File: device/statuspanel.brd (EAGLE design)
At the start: 57.1 x 66 mm, 8 parts

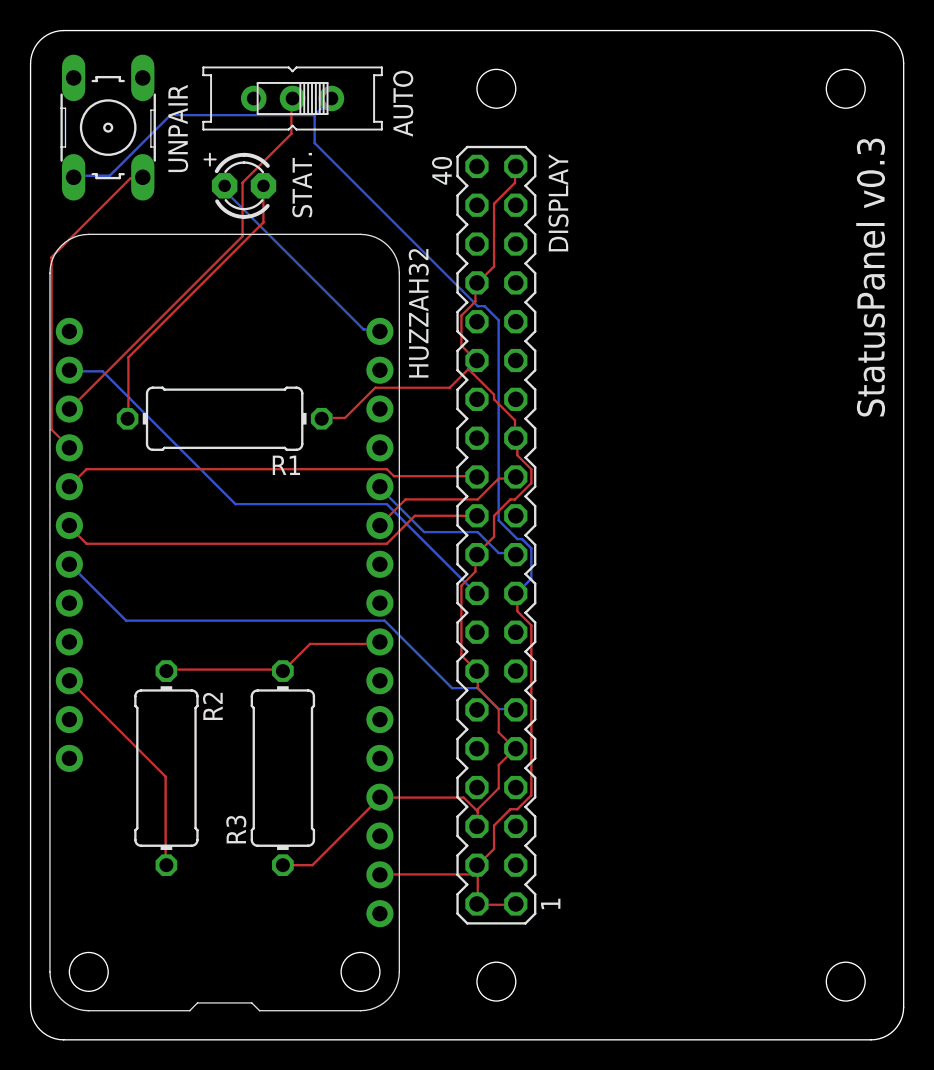
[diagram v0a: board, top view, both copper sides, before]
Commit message: Switching the resistors over to SMD components.
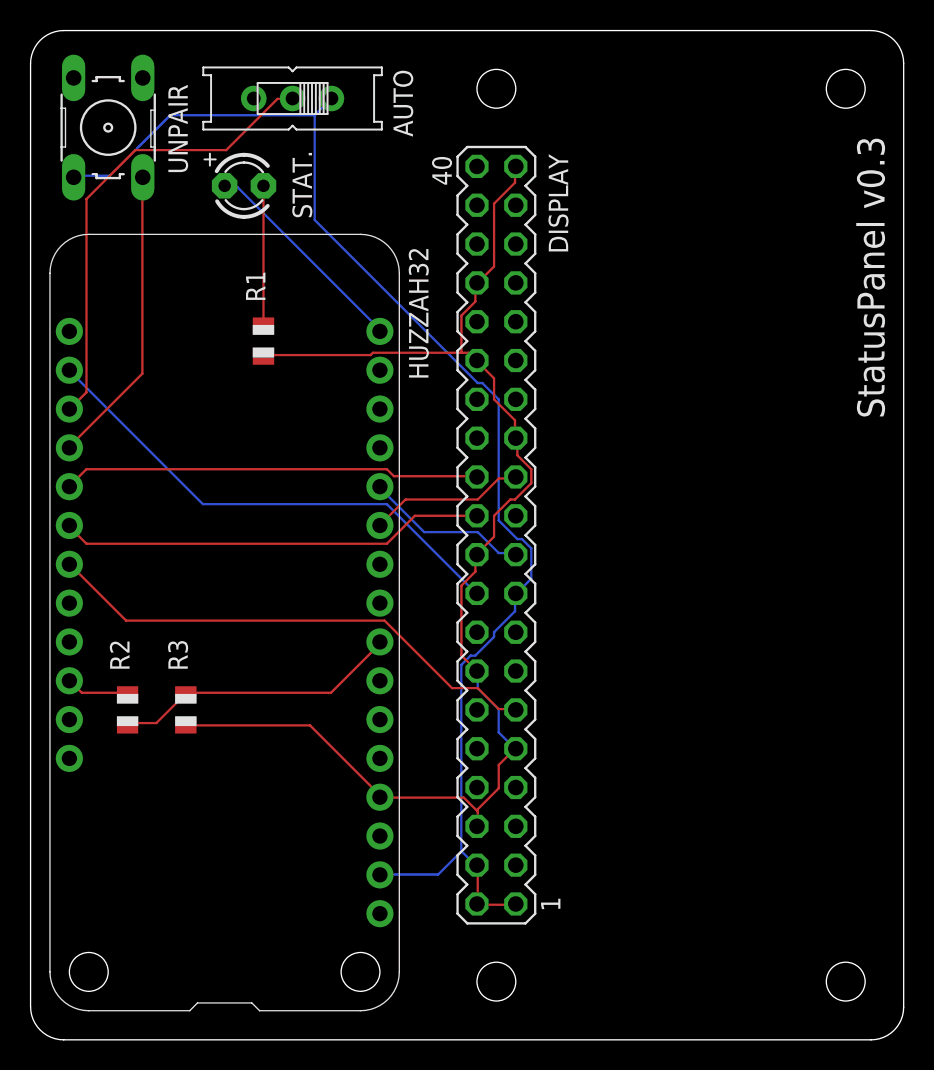
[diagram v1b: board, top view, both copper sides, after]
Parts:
- R1, R2, R3: device adafruit:0411/12 -> adafruit:R0805
- moved R3 7.41 mm to (10.2, 21.6)
- moved R1 5.68 mm to (15.2, 45.7), turned to 90 degrees
- moved R2 4.58 mm to (6.35, 21.6), turned to 90 degrees
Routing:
- net USB: track 14.7 -> 4.19 mm
- net N$3: track 18.9 -> 9.16 mm
- net GND: track 77.7 -> 86.3 mm
- net AUTO: track 26.4 -> 30.4 mm
- net USBDETECT: track 14.9 -> 18.9 mm
- net UNPAIR: track 21.1 -> 19.7 mm
- net 3V3: track 89.2 -> 88.1 mm

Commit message: Add the reset button.
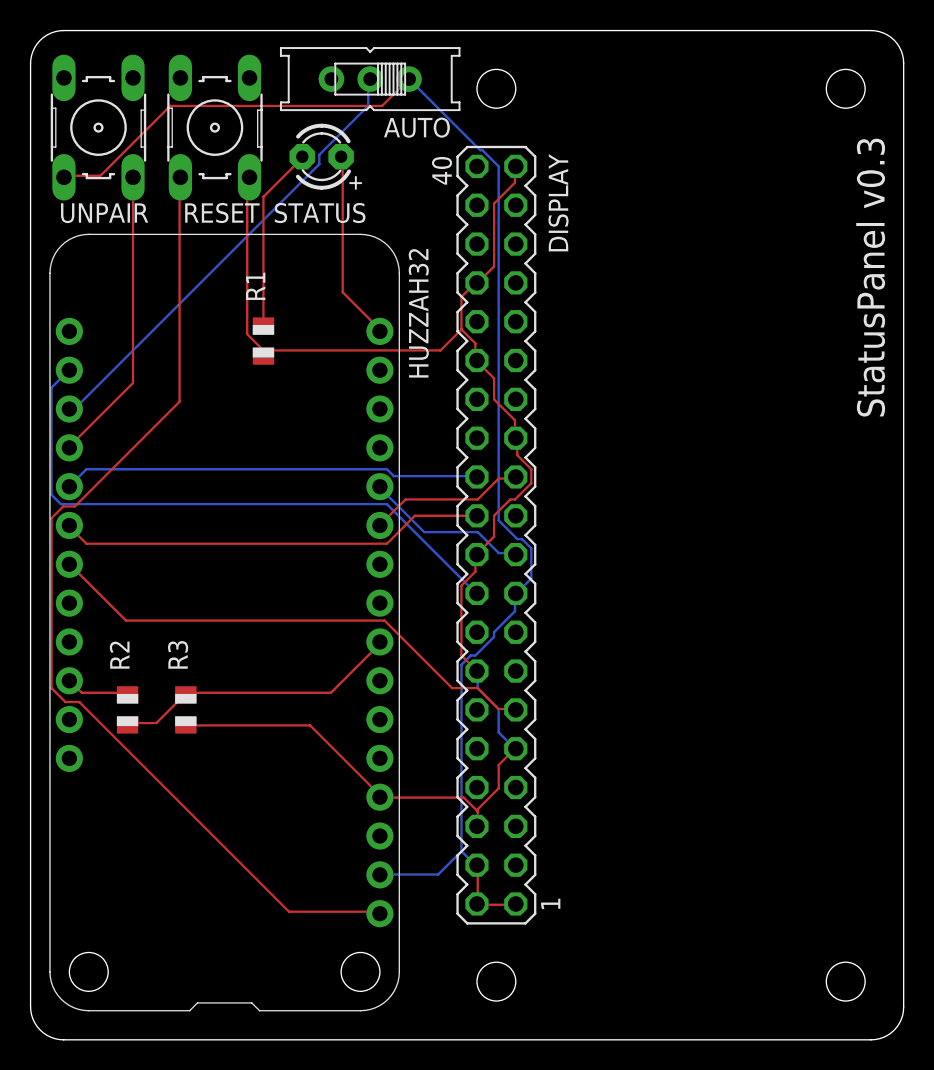
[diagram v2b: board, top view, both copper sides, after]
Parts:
- removed STAT.: (no value), adafruit:LED3MM
- added RESET: (no value), switch-omron:B3F-10XX
- added STATUS: (no value), adafruit:LED3MM
- moved AUTO 5.24 mm to (22.2, 62.9)
- moved UNPAIR 0.63 mm to (4.45, 59.7)
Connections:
- new net RST: HUZZAH32.1, RESET.1
- net GND: now also RESET.3
- net N$3: now also STATUS.K; no longer STAT..K
- net STATUS: now also STATUS.A; no longer STAT..A
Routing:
- net RST: track 0.00 -> 65.0 mm
- net GND: track 86.3 -> 98.7 mm
- net BUSY: track 32.7 -> 39.1 mm
- net 3V3: track 88.1 -> 94.0 mm
- net N$3: track 9.16 -> 12.2 mm
- net STATUS: track 14.2 -> 12.5 mm

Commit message: Update the resistance of the LED resistor.
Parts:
- R1: value 5.1 -> 330
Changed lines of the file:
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@@
 <attribute name="VALUE" x="17.145" y="59.436" size="1.27" layer="27" ratio="10" rot="R180"/>
 </element>
-<element name="R1" library="adafruit" library_urn="urn:adsk.eagle:library:420" package="R0805" package3d_urn="urn:adsk.eagle:package:6240566/1" value="5.1" x="15.24" y="45.72" smashed="yes" rot="R90">
+<element name="R1" library="adafruit" library_urn="urn:adsk.eagle:library:420" package="R0805" package3d_urn="urn:adsk.eagle:package:6240566/1" value="330" x="15.24" y="45.72" smashed="yes" rot="R90">
 <attribute name="NAME" x="15.367" y="48.26" size="1.27" layer="25" ratio="10" rot="R90"/>
 <attribute name="VALUE" x="15.875" y="40.8686" size="1.27" layer="27" ratio="10" rot="R90"/>
